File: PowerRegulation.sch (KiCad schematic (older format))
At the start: 6 parts, among them U301 LM2931

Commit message: added 100uF pcb footprint and misc comments
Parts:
- C302: footprint (none) -> Current:PCE3867CT-ND
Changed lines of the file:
@@
 F 0 "C302" H 6225 3500 50  0000 L CNN
 F 1 "100" H 6225 3300 50  0000 L CNN
-F 2 "" H 6238 3250 50  0000 C CNN
+F 2 "Current:PCE3867CT-ND" H 6238 3250 50  0001 C CNN
 F 3 "https://industrial.panasonic.com/cdbs/www-data/pdf/RDE0000/ABA0000C726.pdf" H 6200 3400 50  0001 C CNN
 F 4 "Value" H 6200 3400 60  0001 C CNN "Fieldname"

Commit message: initial component placement on the pcb
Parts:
- C301: footprint SMD_Packages:SMD-0805 -> Capacitors_SMD:C_0805
- R301, R302, R303: footprint SMD_Packages:SMD-0805 -> Resistors_SMD:R_0805
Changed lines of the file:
@@
 F 0 "R301" V 4280 3200 40  0000 C CNN
 F 1 "0" V 4207 3201 40  0000 C CNN
-F 2 "SMD_Packages:SMD-0805" V 4130 3200 30  0001 C CNN
+F 2 "Resistors_SMD:R_0805" V 4130 3200 30  0001 C CNN
 F 3 "" H 4200 3200 30  0000 C CNN
 F 4 "Value" H 4200 3200 60  0001 C CNN "MPN"
@@
 F 0 "R302" V 5730 2950 40  0000 C CNN
 F 1 "27K" V 5657 2951 40  0000 C CNN
-F 2 "SMD_Packages:SMD-0805" V 5580 2950 30  0001 C CNN
+F 2 "Resistors_SMD:R_0805" V 5580 2950 30  0001 C CNN
 F 3 "" H 5650 2950 30  0000 C CNN
 F 4 "Value" H 5650 2950 60  0001 C CNN "MPN"
@@
 F 0 "R303" V 5730 3550 40  0000 C CNN
 F 1 "21.6K" V 5657 3551 40  0000 C CNN
-F 2 "SMD_Packages:SMD-0805" V 5580 3550 30  0001 C CNN
+F 2 "Resistors_SMD:R_0805" V 5580 3550 30  0001 C CNN
 F 3 "" H 5650 3550 30  0000 C CNN
 	1    5650 3550
@@
 F 0 "C301" H 4025 3350 50  0000 L CNN
 F 1 ".1" H 4025 3150 50  0000 L CNN
-F 2 "SMD_Packages:SMD-0805" H 4038 3100 50  0001 C CNN
+F 2 "Capacitors_SMD:C_0805" H 4038 3100 50  0001 C CNN
 F 3 "" H 4000 3250 50  0000 C CNN
 F 4 "Value" H 4000 3250 60  0001 C CNN "Fieldname"

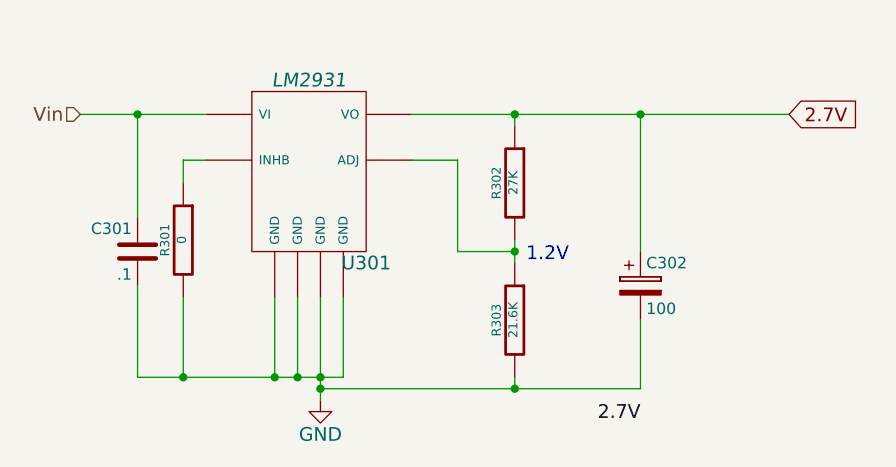
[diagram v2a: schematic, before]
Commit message: added test points to  schematic and pcb
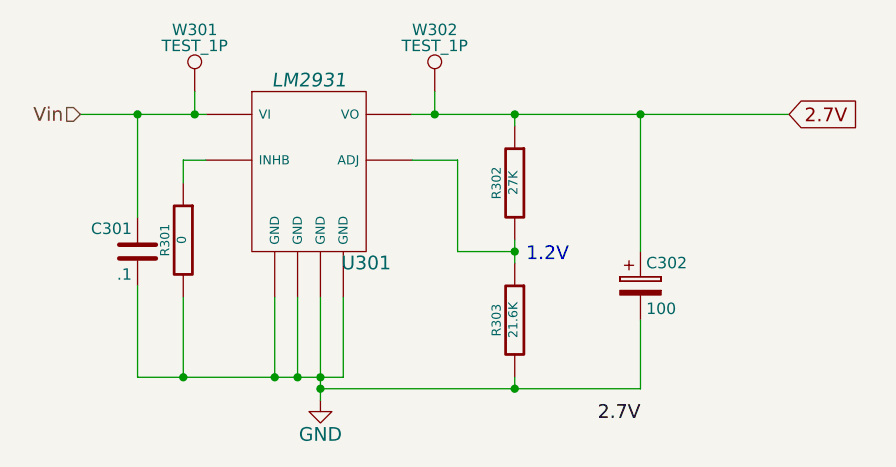
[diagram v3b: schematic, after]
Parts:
- added W301, W302: TEST_1P, Measurement_Points:Measurement_Point_Round-SMD-Pad_Small, symbol TEST_1P
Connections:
- net 2.7V: now also W302.1
- net Vin: now also W301.1
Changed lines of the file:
@@
 Text Notes 5700 3300 0    60   ~ 0
 1.2V\n
+$Comp
+L TEST_1P W302
+U 1 1 57C85635
+P 5300 2550
+F 0 "W302" H 5300 2820 50  0000 C CNN
+F 1 "TEST_1P" H 5300 2750 50  0000 C CNN
+F 2 "Measurement_Points:Measurement_Point_Round-SMD-Pad_Small" H 5500 2550 50  0001 C CNN
+F 3 "" H 5500 2550 50  0000 C CNN
+	1    5300 2550
+	1    0    0    -1
+$EndComp
+Wire Wire Line
+	5300 2550 5300 2650
+Connection ~ 5300 2650
+$Comp
+L TEST_1P W301
+U 1 1 57C856E6
+P 4250 2550
+F 0 "W301" H 4250 2820 50  0000 C CNN
+F 1 "TEST_1P" H 4250 2750 50  0000 C CNN
+F 2 "Measurement_Points:Measurement_Point_Round-SMD-Pad_Small" H 4450 2550 50  0001 C CNN
+F 3 "" H 4450 2550 50  0000 C CNN
+	1    4250 2550
+	1    0    0    -1
+$EndComp
+Wire Wire Line
+	4250 2550 4250 2650
+Connection ~ 4250 2650
 $EndSCHEMATC

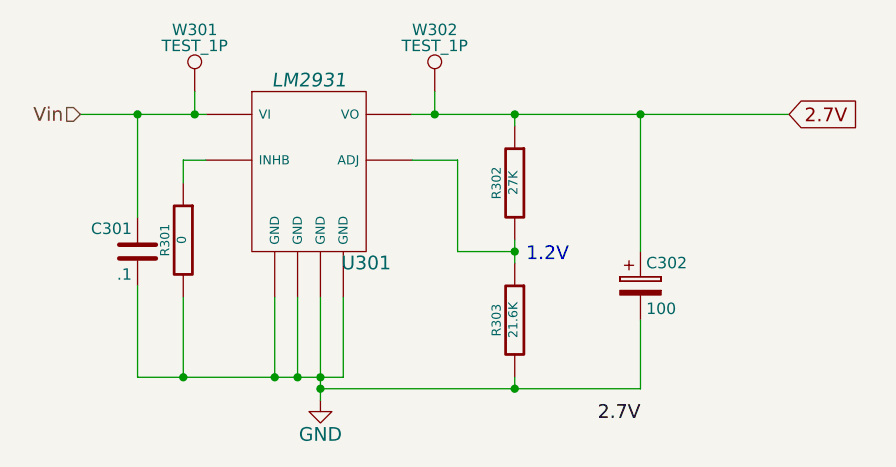
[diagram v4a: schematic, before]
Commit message: revised resistors to match available values, replaced FET (old FET was obsolete/unavail)
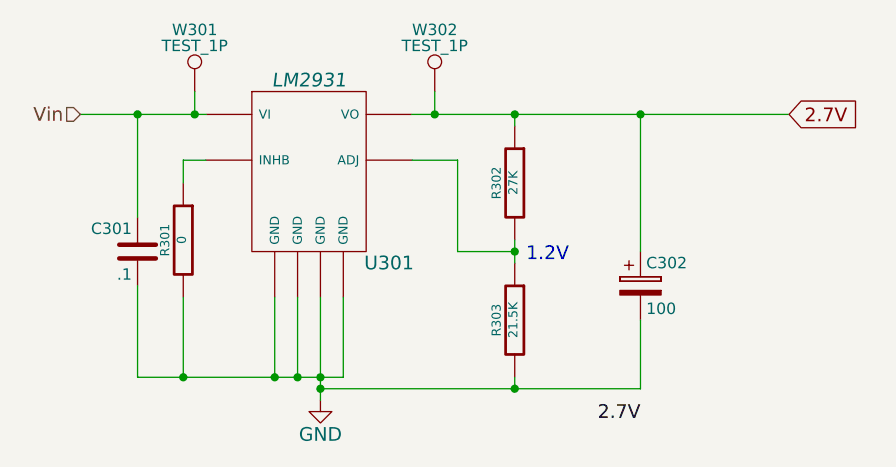
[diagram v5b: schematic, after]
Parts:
- R303: value 21.6K -> 21.5K
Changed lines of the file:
@@
 $EndDescr
 $Comp
-L GND #PWR301
+L GND #PWR05
 U 1 1 54DAF107
 P 4800 3900
-F 0 "#PWR301" H 4800 3650 60  0001 C CNN
+F 0 "#PWR05" H 4800 3650 60  0001 C CNN
 F 1 "GND" H 4800 3750 60  0000 C CNN
 F 2 "" H 4800 3900 60  0000 C CNN
@@
 U 1 1 54DAF12F
 P 4750 3150
-F 0 "U301" H 5000 3000 60  0000 C CNN
+F 0 "U301" H 5100 3000 60  0000 C CNN
 F 1 "LM2931" H 4750 3800 60  0000 C CIN
 F 2 "SMD_Packages:SOIC-8-N" H 4600 3150 60  0001 C CNN
@@
 P 5650 3550
 F 0 "R303" V 5730 3550 40  0000 C CNN
-F 1 "21.6K" V 5657 3551 40  0000 C CNN
+F 1 "21.5K" V 5657 3551 40  0000 C CNN
 F 2 "Resistors_SMD:R_0805" V 5580 3550 30  0001 C CNN
 F 3 "" H 5650 3550 30  0000 C CNN

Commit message: adjusted R303 to get 2.7V, exchanged other parts for availability
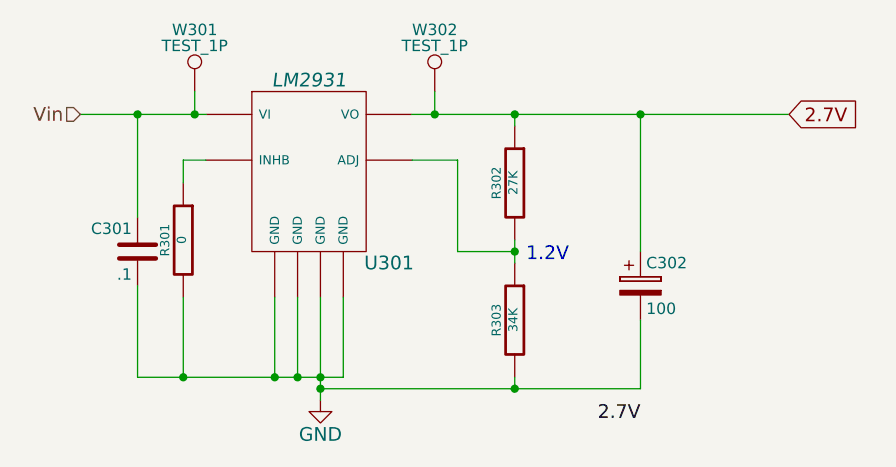
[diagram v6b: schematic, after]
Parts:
- R303: value 21.5K -> 34K
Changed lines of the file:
@@
 P 5650 3550
 F 0 "R303" V 5730 3550 40  0000 C CNN
-F 1 "21.5K" V 5657 3551 40  0000 C CNN
+F 1 "34K" V 5657 3551 40  0000 C CNN
 F 2 "Resistors_SMD:R_0805" V 5580 3550 30  0001 C CNN
 F 3 "" H 5650 3550 30  0000 C CNN
